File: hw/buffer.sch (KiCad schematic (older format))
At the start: 10 parts, among them J6 BNC, U12 OPA859xDSG

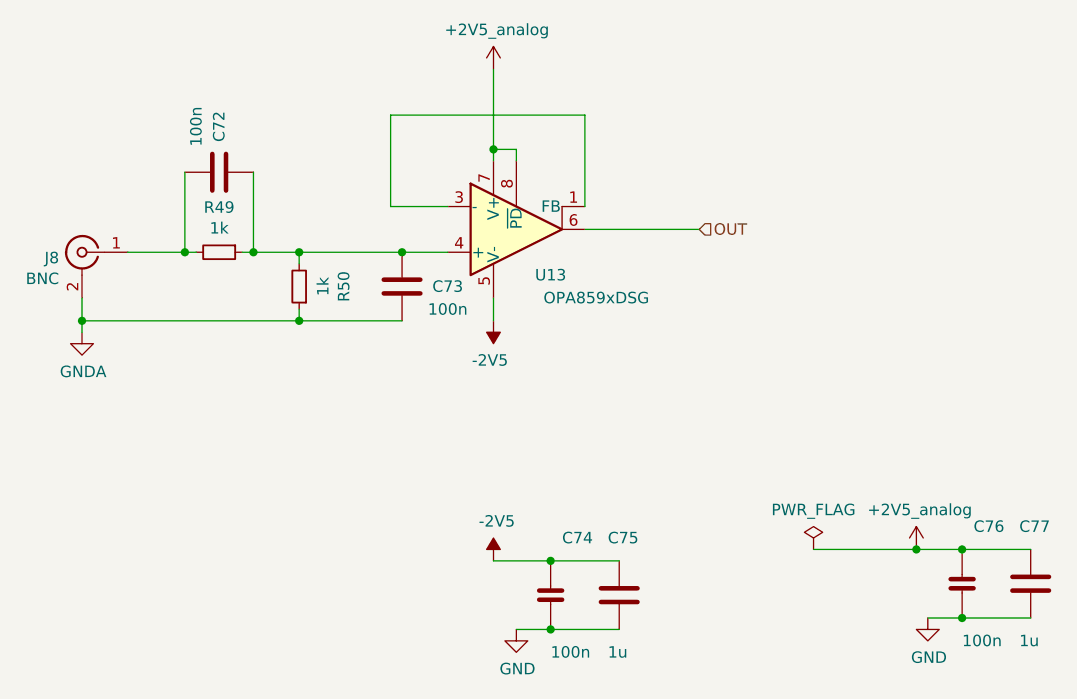
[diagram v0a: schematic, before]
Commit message: added buffer amps for offset dac
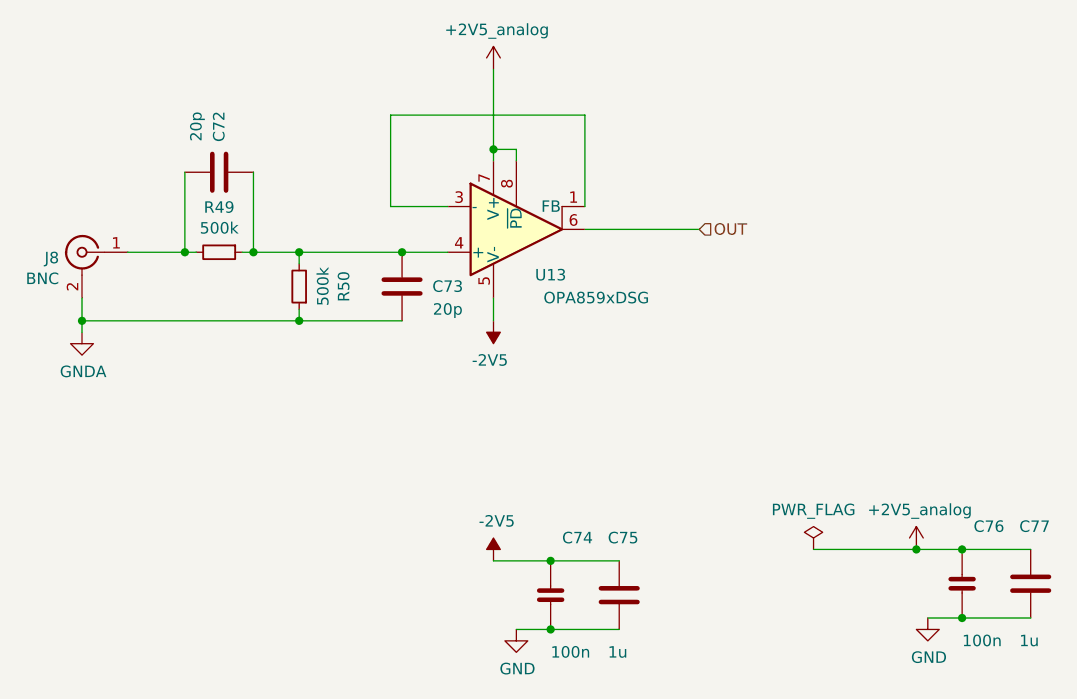
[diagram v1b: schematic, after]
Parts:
- C66, C67: value 100n -> 20p
- R47, R48: value 1k -> 500k
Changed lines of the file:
@@
 $Descr A4 11693 8268
 encoding utf-8
-Sheet 7 7
+Sheet 7 8
 Title ""
 Date ""
@@
 AR Path="/612B1274/611E90A8/611A70F5" Ref="R49"  Part="1"
 F 0 "R49" V 3954 3500 50  0000 C CNN
-F 1 "1k" V 4045 3500 50  0000 C CNN
+F 1 "500k" V 4045 3500 50  0000 C CNN
 F 2 "Resistor_SMD:R_0603_1608Metric" H 4150 3500 50  0001 C CNN
 F 3 "~" H 4150 3500 50  0001 C CNN
@@
 AR Path="/612B1274/611E90A8/61207E57" Ref="C73"  Part="1"
 F 0 "C73" H 5150 3650 50  0000 C CNN
-F 1 "100n" H 5150 3750 50  0000 C CNN
+F 1 "20p" H 5150 3750 50  0000 C CNN
 F 2 "Capacitor_SMD:C_0603_1608Metric" H 4988 3500 50  0001 C CNN
 F 3 "~" H 4950 3650 50  0001 C CNN
@@
 AR Path="/612B1274/611E90A8/61208FD0" Ref="C72"  Part="1"
 F 0 "C72" H 4350 3150 50  0000 C CNN
-F 1 "100n" H 4350 3250 50  0000 C CNN
+F 1 "20p" H 4350 3250 50  0000 C CNN
 F 2 "Capacitor_SMD:C_0603_1608Metric" H 4188 3000 50  0001 C CNN
 F 3 "~" H 4150 3150 50  0001 C CNN
@@
 AR Path="/612B1274/611E90A8/611A713B" Ref="R50"  Part="1"
 F 0 "R50" V 4304 3650 50  0000 C CNN
-F 1 "1k" V 4395 3650 50  0000 C CNN
+F 1 "500k" V 4395 3650 50  0000 C CNN
 F 2 "Resistor_SMD:R_0603_1608Metric" H 4500 3650 50  0001 C CNN
 F 3 "~" H 4500 3650 50  0001 C CNN

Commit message: more work (don't recall details :-()
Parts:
- added C98: 5-15p, proj_footprints:C_Trimmer_EW_Electronics_SCG3S, symbol Device:CTRIM_Small
- C66: Part GCJ188R71E104KA12D -> (none)
- C67: value 20p -> 10p; Part GCJ188R71E104KA12D -> (none)
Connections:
- net GND is gone; now on net GNDA: C68.2, C69.2, C70.2, C71.2
- net GNDA: now also C98.2
- net at C66.2, C67.2, R47.1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: now also C98.1
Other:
- moved on the sheet: U12
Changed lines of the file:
@@
 $Descr A4 11693 8268
 encoding utf-8
-Sheet 7 8
+Sheet 6 8
 Title ""
 Date ""
@@
 L Amplifier_Operational:OPA859xDSG U12
 U 1 1 61178C80
-P 5450 3400
+P 6350 3400
 AR Path="/612B1274/611783BC/61178C80" Ref="U12"  Part="1"
 AR Path="/612B1274/611E90A8/61178C80" Ref="U13"  Part="1"
-F 0 "U13" H 5600 3200 50  0000 C CNN
-F 1 "OPA859xDSG" H 5800 3100 50  0000 C CNN
-F 2 "Package_SON:WSON-8-1EP_2x2mm_P0.5mm_EP0.9x1.6mm" H 5350 4000 50  0001 C CNN
-F 3 "http://www.ti.com/lit/ds/symlink/opa859.pdf" H 5850 3800 50  0001 C CNN
-	1    5450 3400
+F 0 "U12" H 6500 3200 50  0000 C CNN
+F 1 "OPA859xDSG" H 6700 3100 50  0000 C CNN
+F 2 "Package_SON:WSON-8-1EP_2x2mm_P0.5mm_EP0.9x1.6mm" H 6250 4000 50  0001 C CNN
+F 3 "http://www.ti.com/lit/ds/symlink/opa859.pdf" H 6750 3800 50  0001 C CNN
+	1    6350 3400
 	1    0    0    -1
 $EndComp
@@
 AR Path="/612B1274/611783BC/611A4FDB" Ref="J6"  Part="1"
 AR Path="/612B1274/611E90A8/611A4FDB" Ref="J8"  Part="1"
-F 0 "J8" H 3650 3475 50  0000 L CNN
+F 0 "J6" H 3650 3475 50  0000 L CNN
 F 1 "BNC" H 3650 3384 50  0000 L CNN
 F 2 "proj_footprints:BNC_Molex_0731713150" H 3550 3500 50  0001 C CNN
@@
 AR Path="/612B1274/611783BC/611A70F5" Ref="R47"  Part="1"
 AR Path="/612B1274/611E90A8/611A70F5" Ref="R49"  Part="1"
-F 0 "R49" V 3954 3500 50  0000 C CNN
+F 0 "R47" V 3954 3500 50  0000 C CNN
 F 1 "500k" V 4045 3500 50  0000 C CNN
 F 2 "Resistor_SMD:R_0603_1608Metric" H 4150 3500 50  0001 C CNN
@@
 	4250 3500 4300 3500
 Wire Wire Line
-	5150 3300 4900 3300
-Wire Wire Line
-	4900 3300 4900 2900
-Wire Wire Line
-	4900 2900 5750 2900
-Wire Wire Line
-	5750 2900 5750 3300
+	6050 3300 5800 3300
+Wire Wire Line
+	5800 2900 6650 2900
+Wire Wire Line
+	6650 2900 6650 3300
 $Comp
 L power:-2V5 #PWR?
 U 1 1 611CC3FB
-P 5350 3800
+P 6250 3800
 AR Path="/6086F2E3/611CC3FB" Ref="#PWR?"  Part="1"
 AR Path="/612B1274/611783BC/611CC3FB" Ref="#PWR?"  Part="1"
 AR Path="/612B1274/611E90A8/611CC3FB" Ref="#PWR?"  Part="1"
-F 0 "#PWR?" H 5350 3900 50  0001 C CNN
-F 1 "-2V5" H 5365 3973 50  0000 C CNN
-F 2 "" H 5350 3800 50  0001 C CNN
-F 3 "" H 5350 3800 50  0001 C CNN
-	1    5350 3800
+F 0 "#PWR?" H 6250 3900 50  0001 C CNN
+F 1 "-2V5" H 6265 3973 50  0000 C CNN
+F 2 "" H 6250 3800 50  0001 C CNN
+F 3 "" H 6250 3800 50  0001 C CNN
+	1    6250 3800
 	-1   0    0    1
 $EndComp
 Wire Wire Line
-	5350 3700 5350 3800
+	6250 3700 6250 3800
 $Comp
 L fmc:+2V5_analog #PWR?
 U 1 1 611CD651
-P 5350 2700
+P 6250 2700
 AR Path="/612B1274/611783BC/611CD651" Ref="#PWR?"  Part="1"
 AR Path="/612B1274/611E90A8/611CD651" Ref="#PWR?"  Part="1"
-F 0 "#PWR?" H 5350 2550 50  0001 C CNN
-F 1 "+2V5_analog" H 5365 2873 50  0000 C CNN
-F 2 "" H 5350 2700 50  0001 C CNN
-F 3 "" H 5350 2700 50  0001 C CNN
-	1    5350 2700
-	1    0    0    -1
-$EndComp
-Wire Wire Line
-	5350 2700 5350 3050
-Wire Wire Line
-	5450 3100 5450 3050
-Wire Wire Line
-	5450 3050 5350 3050
-Connection ~ 5350 3050
-Wire Wire Line
-	5350 3050 5350 3100
-$Comp
-L power:GND #PWR?
-U 1 1 611D1DD5
-P 7250 5100
-AR Path="/6086F2E3/611D1DD5" Ref="#PWR?"  Part="1"
-AR Path="/60AABC24/611D1DD5" Ref="#PWR?"  Part="1"
-AR Path="/60B16D71/611D1DD5" Ref="#PWR?"  Part="1"
-AR Path="/612B1274/611D1DD5" Ref="#PWR?"  Part="1"
-AR Path="/612B1274/611783BC/611D1DD5" Ref="#PWR?"  Part="1"
-AR Path="/612B1274/611E90A8/611D1DD5" Ref="#PWR?"  Part="1"
-F 0 "#PWR?" H 7250 4850 50  0001 C CNN
-F 1 "GND" H 7255 4927 50  0000 C CNN
-F 2 "" H 7250 5100 50  0001 C CNN
-F 3 "" H 7250 5100 50  0001 C CNN
-	1    7250 5100
-	1    0    0    -1
-$EndComp
-$Comp
-L power:PWR_FLAG #FLG?
-U 1 1 611D1DDB
-P 6750 4800
-AR Path="/612B1274/611D1DDB" Ref="#FLG?"  Part="1"
-AR Path="/612B1274/611783BC/611D1DDB" Ref="#FLG?"  Part="1"
-AR Path="/612B1274/611E90A8/611D1DDB" Ref="#FLG?"  Part="1"
-F 0 "#FLG?" H 6750 4875 50  0001 C CNN
-F 1 "PWR_FLAG" H 6750 4973 50  0000 C CNN
-F 2 "" H 6750 4800 50  0001 C CNN
-F 3 "~" H 6750 4800 50  0001 C CNN
-	1    6750 4800
-	1    0    0    -1
-$EndComp
+F 0 "#PWR?" H 6250 2550 50  0001 C CNN
+F 1 "+2V5_analog" H 6265 2873 50  0000 C CNN
+F 2 "" H 6250 2700 50  0001 C CNN
+F 3 "" H 6250 2700 50  0001 C CNN
+	1    6250 2700
+	1    0    0    -1
+$EndComp
+Wire Wire Line
+	6250 2700 6250 3050
+Wire Wire Line
+	6350 3100 6350 3050
+Wire Wire Line
+	6350 3050 6250 3050
+Connection ~ 6250 3050
+Wire Wire Line
+	6250 3050 6250 3100
 Wire Wire Line
 	7250 5100 7400 5100
@@
 AR Path="/612B1274/611783BC/611D1DE7" Ref="C70"  Part="1"
 AR Path="/612B1274/611E90A8/611D1DE7" Ref="C76"  Part="1"
-F 0 "C76" H 7450 5200 50  0000 L CNN
+F 0 "C70" H 7450 5200 50  0000 L CNN
 F 1 "100n" H 7400 4700 50  0000 L CNN
 F 2 "Capacitor_SMD:C_0402_1005Metric" H 7438 4800 50  0001 C CNN
@@
 Wire Wire Line
 	7400 5100 7700 5100
-Wire Wire Line
-	6750 4800 7200 4800
 $Comp
 L fmc:+2V5_analog #PWR?
@@
 	1    0    0    -1
 $EndComp
-Connection ~ 7200 4800
 Wire Wire Line
 	7200 4800 7400 4800
@@
 AR Path="/612B1274/611783BC/611D4AAD" Ref="C71"  Part="1"
 AR Path="/612B1274/611E90A8/611D4AAD" Ref="C77"  Part="1"
-F 0 "C77" H 7650 5200 50  0000 L CNN
+F 0 "C71" H 7650 5200 50  0000 L CNN
 F 1 "1u" H 7650 4700 50  0000 L CNN
 F 2 "Capacitor_SMD:C_0805_2012Metric" H 7738 4800 50  0001 C CNN
@@
 F 5 "Murata" H 7925 5250 50  0001 C CNN "Manufacturer"
 	1    7700 4950
-	1    0    0    -1
-$EndComp
-$Comp
-L power:GND #PWR?
-U 1 1 611D521B
-P 5450 5150
-AR Path="/6086F2E3/611D521B" Ref="#PWR?"  Part="1"
-AR Path="/60AABC24/611D521B" Ref="#PWR?"  Part="1"
-AR Path="/60B16D71/611D521B" Ref="#PWR?"  Part="1"
-AR Path="/612B1274/611D521B" Ref="#PWR?"  Part="1"
-AR Path="/612B1274/611783BC/611D521B" Ref="#PWR?"  Part="1"
-AR Path="/612B1274/611E90A8/611D521B" Ref="#PWR?"  Part="1"
-F 0 "#PWR?" H 5450 4900 50  0001 C CNN
-F 1 "GND" H 5455 4977 50  0000 C CNN
-F 2 "" H 5450 5150 50  0001 C CNN
-F 3 "" H 5450 5150 50  0001 C CNN
-	1    5450 5150
 	1    0    0    -1
 $EndComp
@@
 AR Path="/612B1274/611783BC/611D5312" Ref="C68"  Part="1"
 AR Path="/612B1274/611E90A8/611D5312" Ref="C74"  Part="1"
-F 0 "C74" H 5650 5250 50  0000 L CNN
+F 0 "C68" H 5650 5250 50  0000 L CNN
 F 1 "100n" H 5600 4750 50  0000 L CNN
 F 2 "Capacitor_SMD:C_0402_1005Metric" H 5638 4850 50  0001 C CNN
@@
 AR Path="/612B1274/611783BC/611D532F" Ref="C69"  Part="1"
 AR Path="/612B1274/611E90A8/611D532F" Ref="C75"  Part="1"
-F 0 "C75" H 5850 5250 50  0000 L CNN
+F 0 "C69" H 5850 5250 50  0000 L CNN
 F 1 "1u" H 5850 4750 50  0000 L CNN
 F 2 "Capacitor_SMD:C_0805_2012Metric" H 5938 4850 50  0001 C CNN
@@
 Wire Wire Line
 	5350 4850 5600 4850
-Text HLabel 6250 3400 2    50   Input ~ 0
+Text HLabel 7150 3400 2    50   Input ~ 0
 OUT
 Wire Wire Line
-	6250 3400 5750 3400
+	7150 3400 6650 3400
 $Comp
 L fmc:100nF_603 C?
@@
 AR Path="/612B1274/611783BC/61207E57" Ref="C67"  Part="1"
 AR Path="/612B1274/611E90A8/61207E57" Ref="C73"  Part="1"
-F 0 "C73" H 5150 3650 50  0000 C CNN
-F 1 "20p" H 5150 3750 50  0000 C CNN
+F 0 "C67" H 5150 3650 50  0000 C CNN
+F 1 "10p" H 5150 3750 50  0000 C CNN
 F 2 "Capacitor_SMD:C_0603_1608Metric" H 4988 3500 50  0001 C CNN
 F 3 "~" H 4950 3650 50  0001 C CNN
-F 4 "GCJ188R71E104KA12D" H 5075 3850 50  0001 C CNN "Part"
+F 4 "" H 5075 3850 50  0001 C CNN "Part"
 F 5 "Murata" H 5175 3950 50  0001 C CNN "Manufacturer"
 	1    4950 3650
 	1    0    0    1
 $EndComp
-Connection ~ 4950 3500
 $Comp
 L fmc:100nF_603 C?
@@
 AR Path="/612B1274/611783BC/61208FD0" Ref="C66"  Part="1"
 AR Path="/612B1274/611E90A8/61208FD0" Ref="C72"  Part="1"
-F 0 "C72" H 4350 3150 50  0000 C CNN
+F 0 "C66" H 4350 3150 50  0000 C CNN
 F 1 "20p" H 4350 3250 50  0000 C CNN
 F 2 "Capacitor_SMD:C_0603_1608Metric" H 4188 3000 50  0001 C CNN
 F 3 "~" H 4150 3150 50  0001 C CNN
-F 4 "GCJ188R71E104KA12D" H 4275 3350 50  0001 C CNN "Part"
+F 4 "" H 4275 3350 50  0001 C CNN "Part"
 F 5 "Murata" H 4375 3450 50  0001 C CNN "Manufacturer"
 	1    4150 3150
@@
 Wire Wire Line
 	4000 3500 4050 3500
-Wire Wire Line
-	4950 3500 5150 3500
 Wire Wire Line
 	3550 3800 3550 3700
@@
 AR Path="/612B1274/611783BC/611A713B" Ref="R48"  Part="1"
 AR Path="/612B1274/611E90A8/611A713B" Ref="R50"  Part="1"
-F 0 "R50" V 4304 3650 50  0000 C CNN
+F 0 "R48" V 4304 3650 50  0000 C CNN
 F 1 "500k" V 4395 3650 50  0000 C CNN
 F 2 "Resistor_SMD:R_0603_1608Metric" H 4500 3650 50  0001 C CNN
@@
 Wire Wire Line
 	4500 3800 4950 3800
+$Comp
+L Device:CTRIM_Small C98
+U 1 1 60D14E8F
+P 5350 3650
+AR Path="/612B1274/611783BC/60D14E8F" Ref="C98"  Part="1"
+AR Path="/612B1274/611E90A8/60D14E8F" Ref="C99"  Part="1"
+F 0 "C98" H 5441 3696 50  0000 L CNN
+F 1 "5-15p" H 5441 3605 50  0000 L CNN
+F 2 "proj_footprints:C_Trimmer_EW_Electronics_SCG3S" H 5350 3650 50  0001 C CNN
+F 3 "~" H 5350 3650 50  0001 C CNN
+	1    5350 3650
+	1    0    0    -1
+$EndComp
+Wire Wire Line
+	4950 3500 5350 3500
+Connection ~ 4950 3500
+Wire Wire Line
+	4950 3800 5350 3800
+Wire Wire Line
+	5350 3800 5350 3750
+Connection ~ 4950 3800
+Wire Wire Line
+	5350 3550 5350 3500
+Connection ~ 5350 3500
+Wire Wire Line
+	5350 3500 6050 3500
+Wire Wire Line
+	5800 2900 5800 3300
+$Comp
+L power:GNDA #PWR?
+U 1 1 60D1F160
+P 5450 5150
+AR Path="/612B1274/60D1F160" Ref="#PWR?"  Part="1"
+AR Path="/612B1274/611783BC/60D1F160" Ref="#PWR?"  Part="1"
+AR Path="/612B1274/611E90A8/60D1F160" Ref="#PWR?"  Part="1"
+F 0 "#PWR?" H 5450 4900 50  0001 C CNN
+F 1 "GNDA" H 5455 4977 50  0000 C CNN
+F 2 "" H 5450 5150 50  0001 C CNN
+F 3 "" H 5450 5150 50  0001 C CNN
+	1    5450 5150
+	1    0    0    -1
+$EndComp
+$Comp
+L power:GNDA #PWR?
+U 1 1 60D1F949
+P 7250 5100
+AR Path="/612B1274/60D1F949" Ref="#PWR?"  Part="1"
+AR Path="/612B1274/611783BC/60D1F949" Ref="#PWR?"  Part="1"
+AR Path="/612B1274/611E90A8/60D1F949" Ref="#PWR?"  Part="1"
+F 0 "#PWR?" H 7250 4850 50  0001 C CNN
+F 1 "GNDA" H 7255 4927 50  0000 C CNN
+F 2 "" H 7250 5100 50  0001 C CNN
+F 3 "" H 7250 5100 50  0001 C CNN
+	1    7250 5100
+	1    0    0    -1
+$EndComp
 $EndSCHEMATC

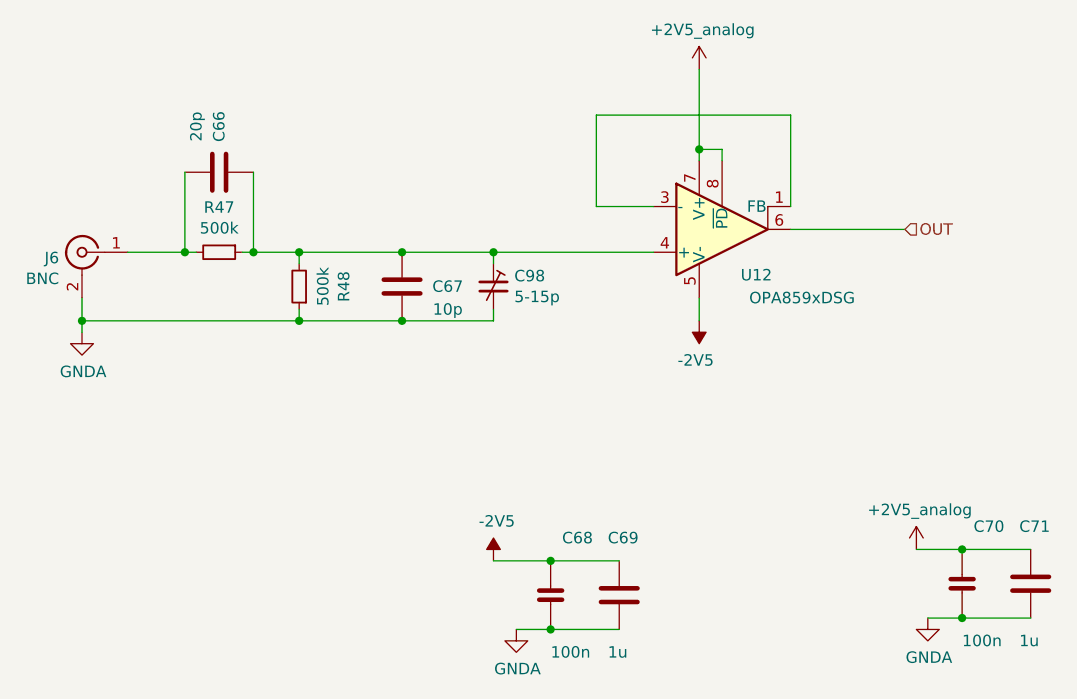
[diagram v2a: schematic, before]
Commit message: everything hooked up + layed out; 0.2/0.4mm vias :-(
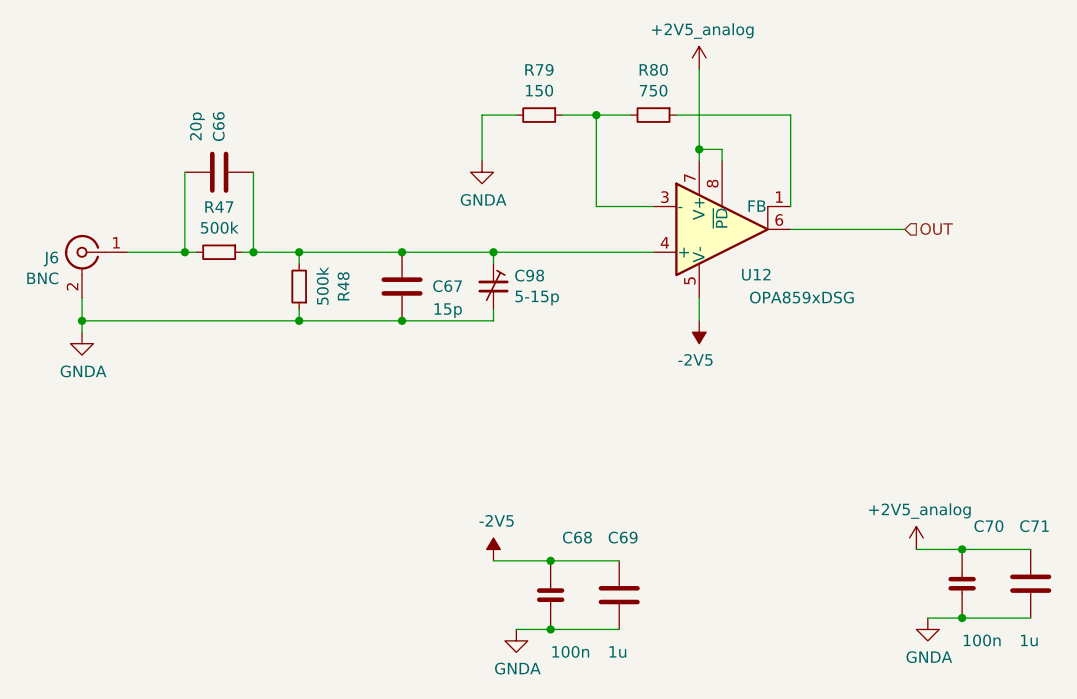
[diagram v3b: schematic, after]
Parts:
- added R81: 150, Resistor_SMD:R_0402_1005Metric, symbol Device:R_Small
- added R82: 750, Resistor_SMD:R_0402_1005Metric, symbol Device:R_Small
- C67: value 10p -> 15p
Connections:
- net GNDA: now also R81.2
- net at U12.1 (FB): now also R82.1; no longer U12.3 (-)
- new net: R81.1, R82.2, U12.3 (-)
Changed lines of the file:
@@
 $Descr A4 11693 8268
 encoding utf-8
-Sheet 6 8
+Sheet 7 9
 Title ""
 Date ""
@@
 	6050 3300 5800 3300
 Wire Wire Line
-	5800 2900 6650 2900
-Wire Wire Line
 	6650 2900 6650 3300
 $Comp
@@
 AR Path="/612B1274/611E90A8/61207E57" Ref="C73"  Part="1"
 F 0 "C67" H 5150 3650 50  0000 C CNN
-F 1 "10p" H 5150 3750 50  0000 C CNN
+F 1 "15p" H 5150 3750 50  0000 C CNN
 F 2 "Capacitor_SMD:C_0603_1608Metric" H 4988 3500 50  0001 C CNN
 F 3 "~" H 4950 3650 50  0001 C CNN
@@
 	1    0    0    -1
 $EndComp
+$Comp
+L Device:R_Small R82
+U 1 1 60F53174
+P 6050 2900
+AR Path="/612B1274/611E90A8/60F53174" Ref="R82"  Part="1"
+AR Path="/612B1274/611783BC/60F53174" Ref="R80"  Part="1"
+F 0 "R80" V 5854 2900 50  0000 C CNN
+F 1 "750" V 5945 2900 50  0000 C CNN
+F 2 "Resistor_SMD:R_0402_1005Metric" H 6050 2900 50  0001 C CNN
+F 3 "~" H 6050 2900 50  0001 C CNN
+	1    6050 2900
+	0    1    1    0
+$EndComp
+$Comp
+L Device:R_Small R81
+U 1 1 60F5371A
+P 5550 2900
+AR Path="/612B1274/611E90A8/60F5371A" Ref="R81"  Part="1"
+AR Path="/612B1274/611783BC/60F5371A" Ref="R79"  Part="1"
+F 0 "R79" V 5354 2900 50  0000 C CNN
+F 1 "150" V 5445 2900 50  0000 C CNN
+F 2 "Resistor_SMD:R_0402_1005Metric" H 5550 2900 50  0001 C CNN
+F 3 "~" H 5550 2900 50  0001 C CNN
+	1    5550 2900
+	0    1    1    0
+$EndComp
+Wire Wire Line
+	6150 2900 6650 2900
+Wire Wire Line
+	5950 2900 5800 2900
+Connection ~ 5800 2900
+Wire Wire Line
+	5800 2900 5650 2900
+$Comp
+L power:GNDA #PWR?
+U 1 1 60F54B66
+P 5300 3100
+AR Path="/612B1274/60F54B66" Ref="#PWR?"  Part="1"
+AR Path="/612B1274/611783BC/60F54B66" Ref="#PWR?"  Part="1"
+AR Path="/612B1274/611E90A8/60F54B66" Ref="#PWR?"  Part="1"
+F 0 "#PWR?" H 5300 2850 50  0001 C CNN
+F 1 "GNDA" H 5305 2927 50  0000 C CNN
+F 2 "" H 5300 3100 50  0001 C CNN
+F 3 "" H 5300 3100 50  0001 C CNN
+	1    5300 3100
+	1    0    0    -1
+$EndComp
+Wire Wire Line
+	5300 3100 5300 2900
+Wire Wire Line
+	5300 2900 5450 2900
 $EndSCHEMATC
